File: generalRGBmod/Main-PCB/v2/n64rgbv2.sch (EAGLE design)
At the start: 76 parts, among them J3 2510-, U1 5M570ZT100C5, U2 ADV7125/ADV7123, U4 TLV70018-DDC

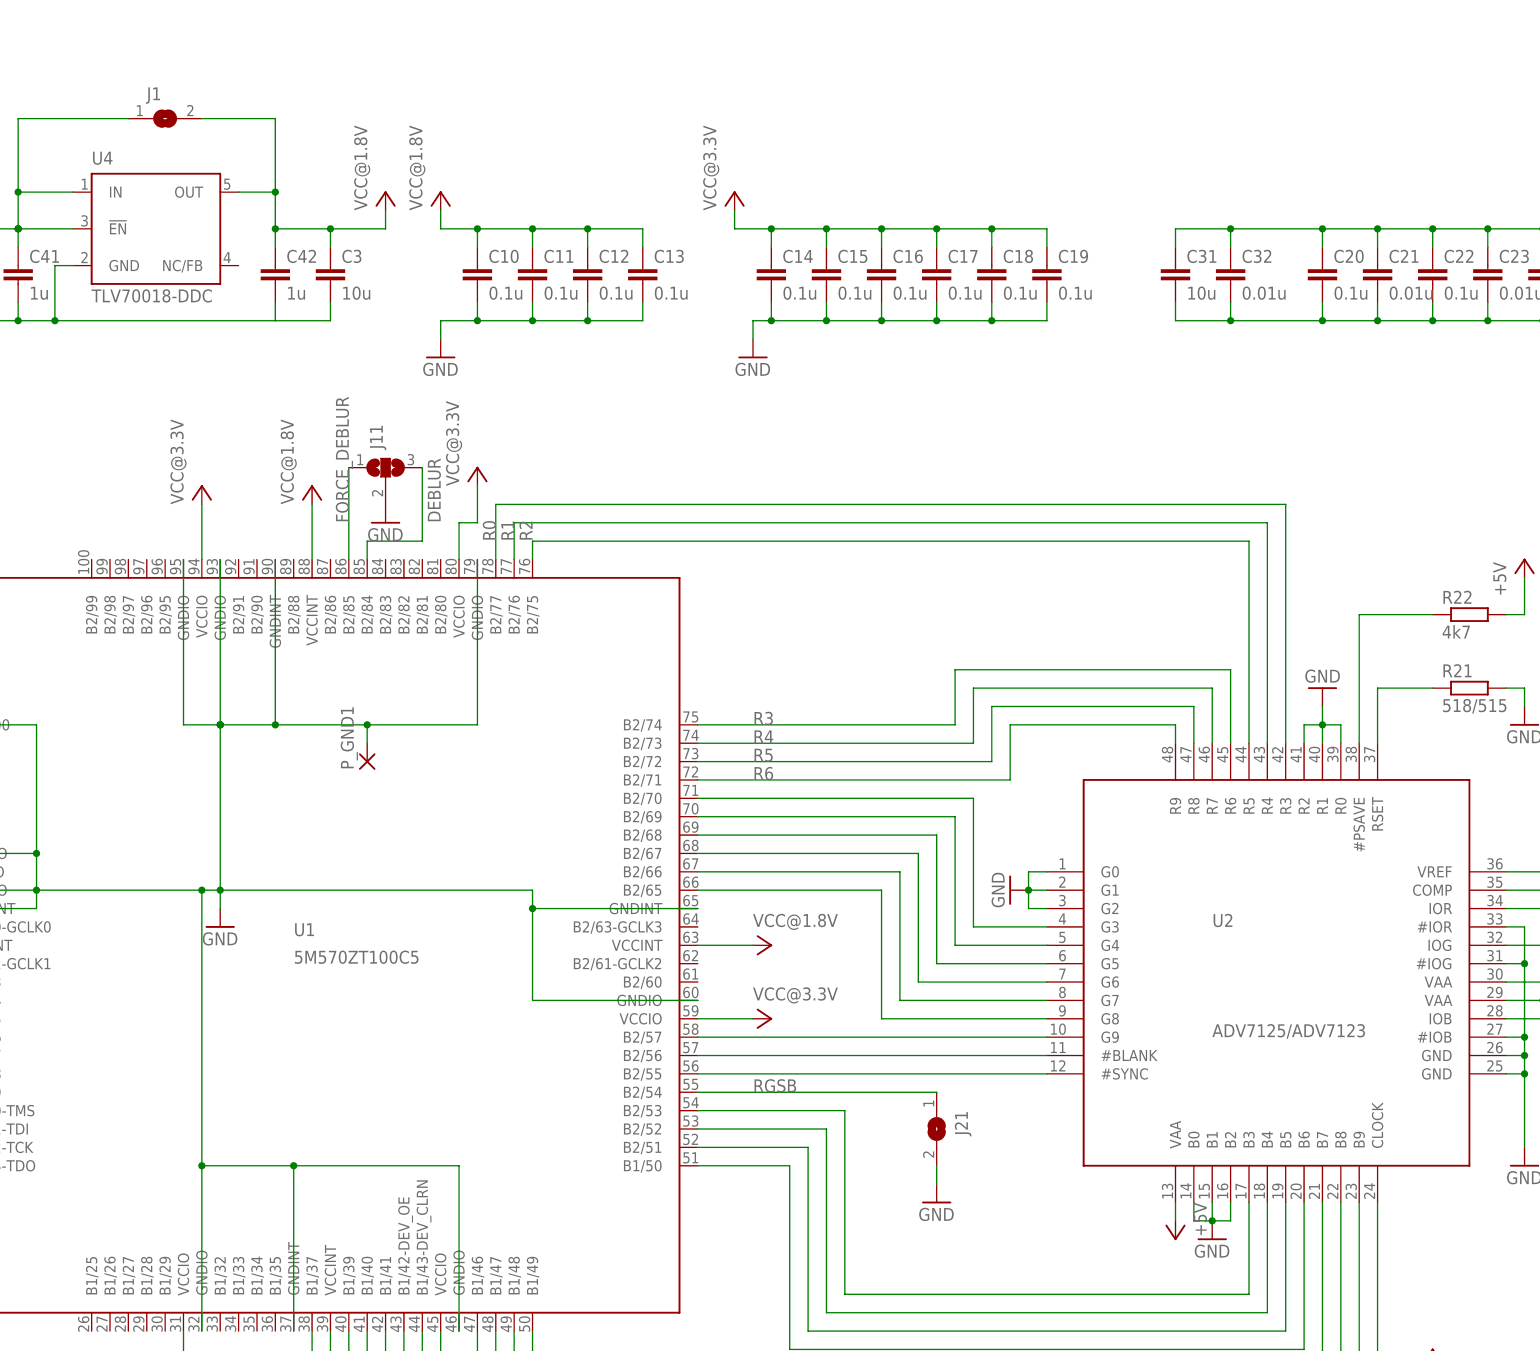
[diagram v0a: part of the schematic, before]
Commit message: use LSB of the ADV7125 (new design is compatible to initial public N64RGBv2 Version 20171211)
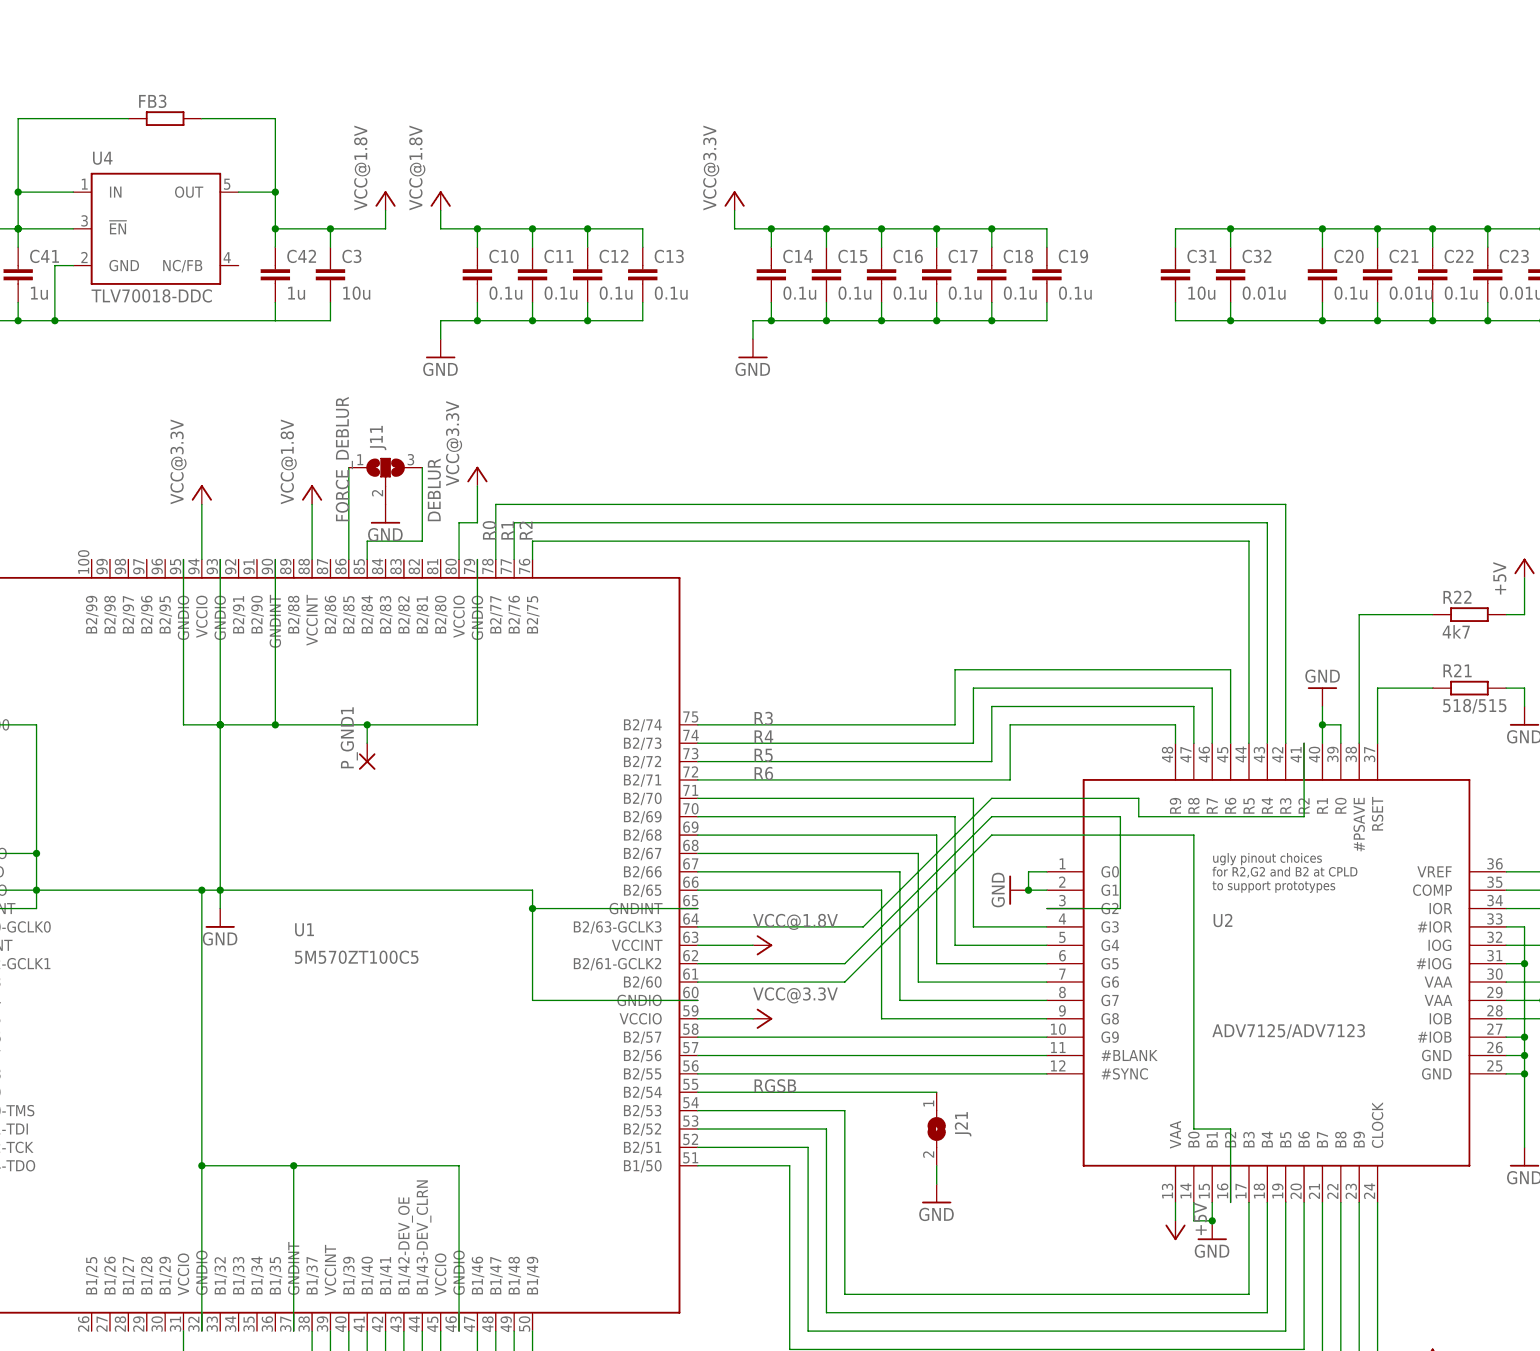
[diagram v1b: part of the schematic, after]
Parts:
- removed J1: (no value), jumper:SJ
- added FB3: (no value), rcl:R-EU_R0603
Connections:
- new net N$25: U1.B2/63-GCLK3, U2.R2
- new net N$41: U1.B2/61-GCLK2, U2.G2
- new net N$43: U1.B2/60, U2.B2
- net GND: no longer U2.B2, U2.G2, U2.R2
- net VCC@1.8V: now also FB3.2; no longer J1.2
- net VCC@3.3V: now also FB3.1; no longer J1.1
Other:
- note added: "ugly pinout choices for R2,G2 and B2 at CPLD to support prototypes"
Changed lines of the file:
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@@
 <?xml version="1.0" encoding="utf-8"?>
 <!DOCTYPE eagle SYSTEM "eagle.dtd">
-<eagle version="8.5.0">
+<eagle version="8.4.3">
 <drawing>
 <settings>
@@
 <part name="J11" library="jumper" deviceset="SJ2W" device=""/>
 <part name="GND18" library="supply1" library_urn="urn:adsk.eagle:library:371" deviceset="GND" device=""/>
-<part name="J1" library="jumper" deviceset="SJ" device=""/>
 <part name="U2" library="analog-devices" deviceset="ADV7123" device="" value="ADV7125/ADV7123"/>
 <part name="AGND10" library="supply1" library_urn="urn:adsk.eagle:library:371" deviceset="GND" device=""/>
@@
 <part name="P_GND3" library="wirepad" deviceset="SMD2" device=""/>
 <part name="J12" library="jumper" deviceset="SJ2W" device=""/>
+<part name="FB3" library="rcl" deviceset="R-EU_" device="R0603"/>
 </parts>
 <sheets>
@@
 <wire x1="91.44" y1="64.77" x2="71.12" y2="64.77" width="0.1524" layer="94"/>
 <wire x1="71.12" y1="64.77" x2="71.12" y2="82.55" width="0.1524" layer="94"/>
+<text x="269.24" y="129.54" size="1.27" layer="97" font="fixed">ugly pinout choices
+for R2,G2 and B2 at CPLD
+to support prototypes</text>
 </plain>
 <instances>
@@
 <instance part="J11" gate="G$1" x="154.94" y="187.96" rot="R90"/>
 <instance part="GND18" gate="1" x="154.94" y="180.34"/>
-<instance part="J1" gate="1" x="124.46" y="236.22"/>
 <instance part="U2" gate="G$1" x="276.86" y="116.84"/>
 <instance part="AGND10" gate="1" x="312.42" y="91.44"/>
@@
 <instance part="P_GND3" gate="1" x="55.88" y="200.66"/>
 <instance part="J12" gate="G$1" x="139.7" y="58.42" rot="R90"/>
+<instance part="FB3" gate="G$1" x="124.46" y="236.22"/>
 </instances>
 <busses>
@@
 <wire x1="266.7" y1="83.82" x2="269.24" y2="83.82" width="0.1524" layer="91"/>
 <junction x="269.24" y="83.82"/>
-<wire x1="269.24" y1="83.82" x2="271.78" y2="83.82" width="0.1524" layer="91"/>
-<pinref part="U2" gate="G$1" pin="B2"/>
-<wire x1="271.78" y1="83.82" x2="271.78" y2="86.36" width="0.1524" layer="91"/>
 </segment>
 <segment>
@@
 <wire x1="287.02" y1="152.4" x2="284.48" y2="152.4" width="0.1524" layer="91"/>
 <junction x="284.48" y="152.4"/>
-<wire x1="284.48" y1="152.4" x2="281.94" y2="152.4" width="0.1524" layer="91"/>
-<pinref part="U2" gate="G$1" pin="R2"/>
-<wire x1="281.94" y1="152.4" x2="281.94" y2="149.86" width="0.1524" layer="91"/>
 </segment>
 <segment>
@@
 <wire x1="246.38" y1="129.54" x2="243.84" y2="129.54" width="0.1524" layer="91"/>
 <junction x="243.84" y="129.54"/>
-<pinref part="U2" gate="G$1" pin="G2"/>
-<wire x1="246.38" y1="127" x2="243.84" y2="127" width="0.1524" layer="91"/>
-<wire x1="243.84" y1="127" x2="243.84" y2="129.54" width="0.1524" layer="91"/>
 </segment>
 <segment>
@@
 <junction x="104.14" y="226.06"/>
 <wire x1="104.14" y1="236.22" x2="119.38" y2="236.22" width="0.1524" layer="91"/>
-<pinref part="J1" gate="1" pin="1"/>
+<pinref part="FB3" gate="G$1" pin="1"/>
 </segment>
 <segment>
@@
 <wire x1="139.7" y1="236.22" x2="139.7" y2="226.06" width="0.1524" layer="91"/>
 <junction x="139.7" y="226.06"/>
-<pinref part="J1" gate="1" pin="2"/>
 <pinref part="C3" gate="G$1" pin="1"/>
 <wire x1="147.32" y1="218.44" x2="147.32" y2="220.98" width="0.1524" layer="91"/>
 <junction x="147.32" y="220.98"/>
+<pinref part="FB3" gate="G$1" pin="2"/>
 </segment>
 <segment>
@@
 </segment>
 </net>
+<net name="N$25" class="0">
+<segment>
+<pinref part="U1" gate="G$1" pin="B2/63-GCLK3"/>
+<wire x1="198.12" y1="124.46" x2="220.98" y2="124.46" width="0.1524" layer="91"/>
+<wire x1="220.98" y1="124.46" x2="238.76" y2="142.24" width="0.1524" layer="91"/>
+<wire x1="238.76" y1="142.24" x2="259.08" y2="142.24" width="0.1524" layer="91"/>
+<wire x1="259.08" y1="142.24" x2="259.08" y2="139.7" width="0.1524" layer="91"/>
+<wire x1="259.08" y1="139.7" x2="281.94" y2="139.7" width="0.1524" layer="91"/>
+<pinref part="U2" gate="G$1" pin="R2"/>
+<wire x1="281.94" y1="139.7" x2="281.94" y2="149.86" width="0.1524" layer="91"/>
+</segment>
+</net>
+<net name="N$41" class="0">
+<segment>
+<pinref part="U1" gate="G$1" pin="B2/61-GCLK2"/>
+<wire x1="198.12" y1="119.38" x2="218.44" y2="119.38" width="0.1524" layer="91"/>
+<wire x1="218.44" y1="119.38" x2="238.76" y2="139.7" width="0.1524" layer="91"/>
+<wire x1="238.76" y1="139.7" x2="256.54" y2="139.7" width="0.1524" layer="91"/>
+<wire x1="256.54" y1="139.7" x2="256.54" y2="127" width="0.1524" layer="91"/>
+<pinref part="U2" gate="G$1" pin="G2"/>
+<wire x1="256.54" y1="127" x2="246.38" y2="127" width="0.1524" layer="91"/>
+</segment>
+</net>
+<net name="N$43" class="0">
+<segment>
+<pinref part="U1" gate="G$1" pin="B2/60"/>
+<wire x1="198.12" y1="116.84" x2="218.44" y2="116.84" width="0.1524" layer="91"/>
+<wire x1="218.44" y1="116.84" x2="238.76" y2="137.16" width="0.1524" layer="91"/>
+<wire x1="238.76" y1="137.16" x2="266.7" y2="137.16" width="0.1524" layer="91"/>
+<pinref part="U2" gate="G$1" pin="B2"/>
+<wire x1="271.78" y1="96.52" x2="271.78" y2="86.36" width="0.1524" layer="91"/>
+<wire x1="271.78" y1="96.52" x2="266.7" y2="96.52" width="0.1524" layer="91"/>
+<wire x1="266.7" y1="96.52" x2="266.7" y2="137.16" width="0.1524" layer="91"/>
+</segment>
+</net>
 </nets>
 </sheet>
@@
 </drawing>
 <compatibility>
+<note version="6.3" minversion="6.2.2" severity="warning">
+Since Version 6.2.2 text objects can contain more than one line,
+which will not be processed correctly with this version.
+</note>
 <note version="8.2" severity="warning">
 Since Version 8.2, EAGLE supports online libraries. The ids
